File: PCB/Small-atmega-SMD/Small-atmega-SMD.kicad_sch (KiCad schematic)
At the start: 30 parts, among them J1 Daisy port in, J2 ICSP_ISP6, J3 UART, J4 Daisy port out, K1 HYC77-TF09-200, U1 PC817C-S, U2 SE5218, U21 TXB0104QPWRQ1, U3 ATmega328P-AU, Y1 16MHz

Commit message: Move connector away from MCU
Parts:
- J1: footprint Connector_IDC:IDC-Header_2x10_P2.54mm_Vertical -> Connector_IDC:IDC-Header_2x10_P2.54mm_Horizontal
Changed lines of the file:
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@@
 			)
 		)
-		(property "Footprint" "Connector_IDC:IDC-Header_2x10_P2.54mm_Vertical"
+		(property "Footprint" "Connector_IDC:IDC-Header_2x10_P2.54mm_Horizontal"
 			(at 33.02 31.75 0)
 			(effects

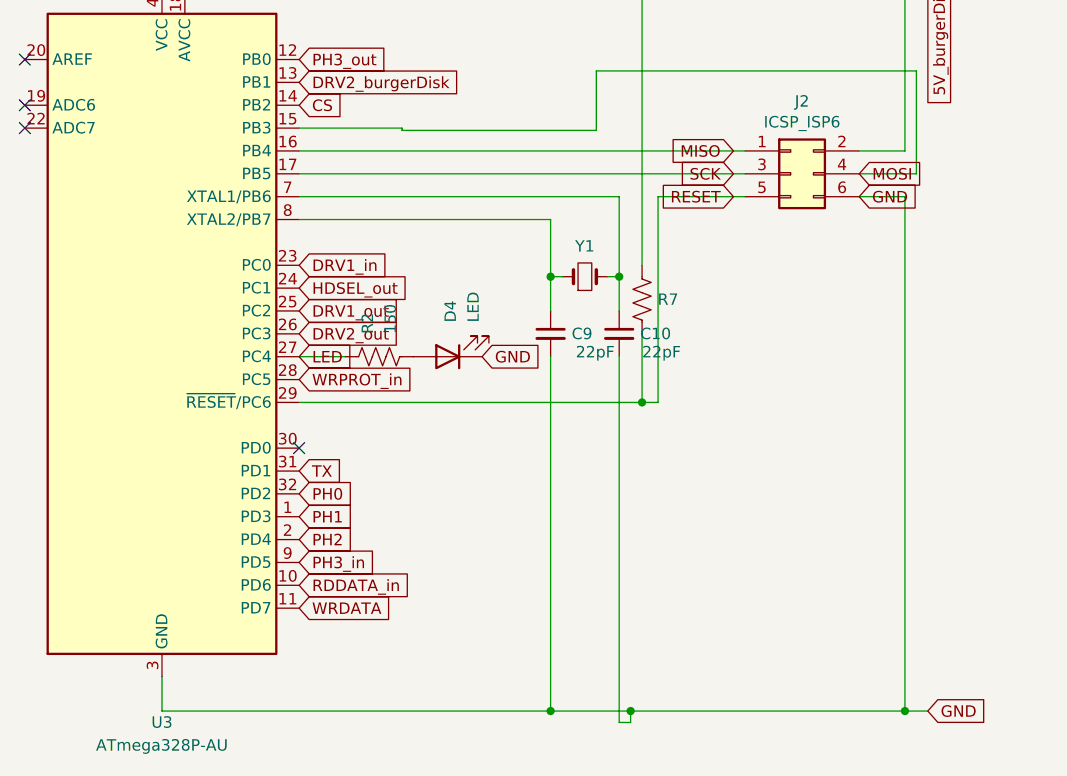
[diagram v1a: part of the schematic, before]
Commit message: Switch to resonator
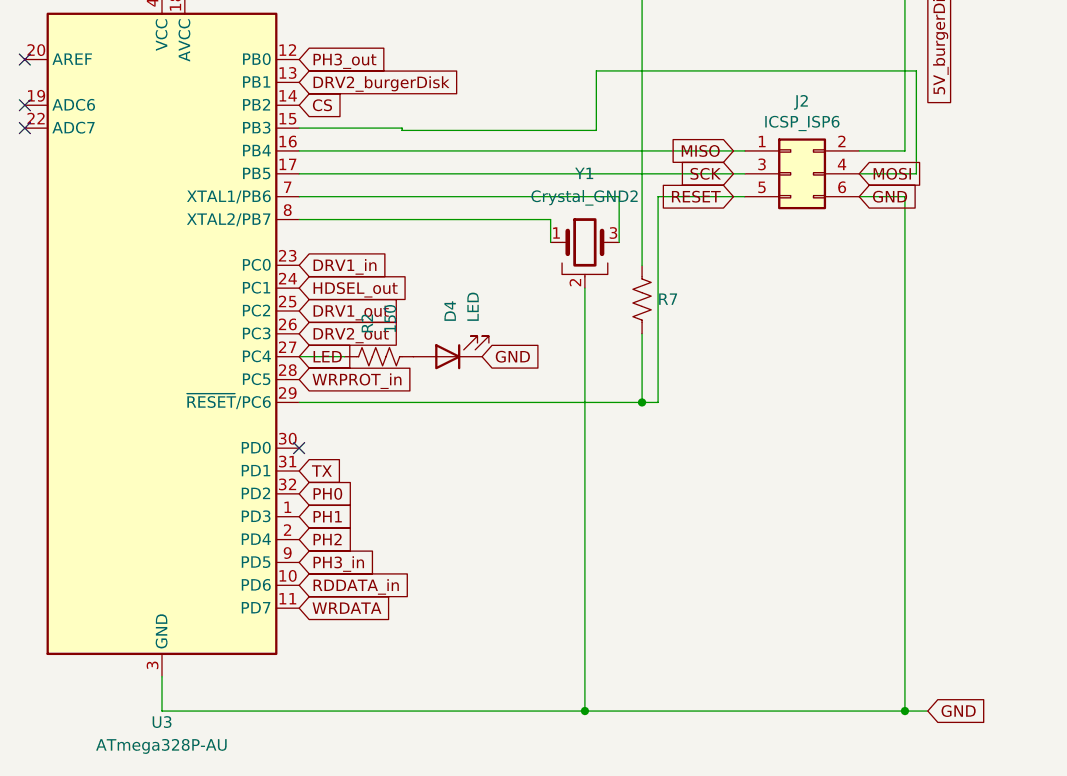
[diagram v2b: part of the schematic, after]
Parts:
- removed C10, C9: 22pF, Capacitor_SMD:C_0603_1608Metric, symbol Device:C_Small
- removed Y1: 16MHz, Crystal:Crystal_SMD_HC49-SD, symbol Device:Crystal_Small
- added Y1: Crystal_GND2, Crystal:Resonator_SMD_Murata_CSTxExxV-3Pin_3.0x1.1mm, symbol Device:Crystal_GND2
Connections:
- net GND: now also Y1.2
- net at U3.8 (XTAL2/PB7): now also Y1.1
- net at U3.7 (XTAL1/PB6): now also Y1.3

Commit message: Rework for cleanliness
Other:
- note removed: "HEADER"

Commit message: Fix part number on Small version
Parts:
- J1: LCSC C3405 -> C9144
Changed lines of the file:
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@@
 			)
 		)
-		(property "LCSC" "C3405"
+		(property "LCSC" "C9144"
 			(at 33.02 31.75 0)
 			(effects

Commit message: Fix LCSC parts
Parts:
- R7: LCSC C17414 -> C177337
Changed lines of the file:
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@@
 			)
 		)
-		(property "LCSC" "C17414"
+		(property "LCSC" "C177337"
 			(at 113.03 127 0)
 			(effects

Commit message: Add libraries and update Domino/Angled
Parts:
- K1: footprint MICROSD-HYC77-TF09-200:MICROSD-HYC77-TF09-200 -> HYC04-TF09-200:MICROSD-HYC77-TF09-200
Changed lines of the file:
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@@
 			)
 		)
-		(property "Footprint" "MICROSD-HYC77-TF09-200:MICROSD-HYC77-TF09-200"
+		(property "Footprint" "HYC04-TF09-200:MICROSD-HYC77-TF09-200"
 			(at -86.36 54.61 0)
 			(effects

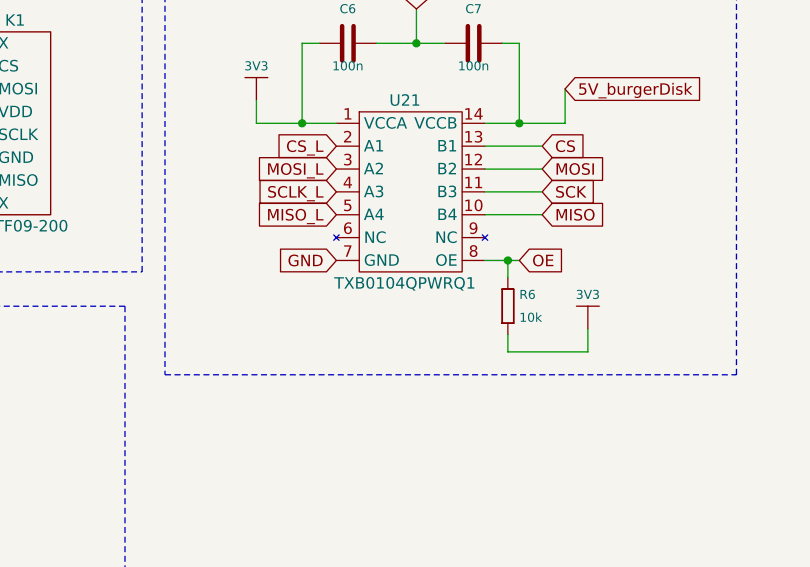
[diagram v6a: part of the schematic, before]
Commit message: Add logo (thanks to Javier Rivera!!)
Add my own micro/SD modules
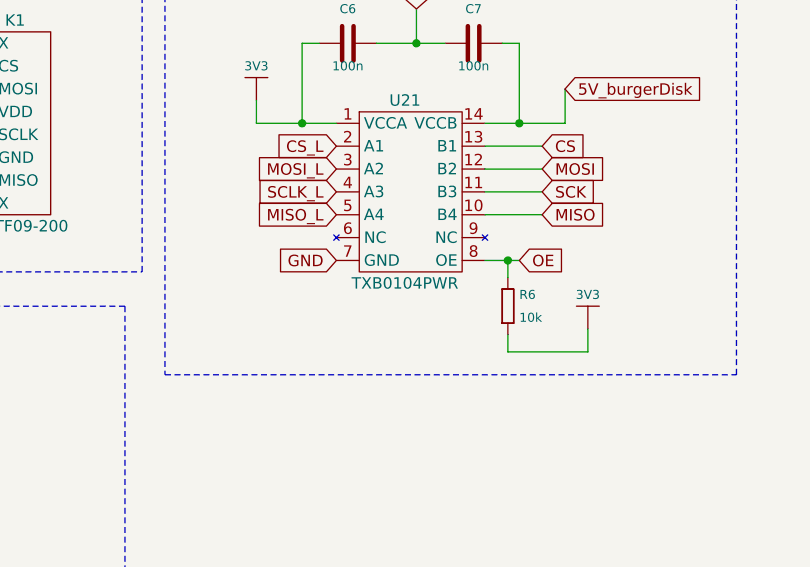
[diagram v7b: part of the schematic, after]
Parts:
- U21: value TXB0104QPWRQ1 -> TXB0104PWR; LCSC C527571 -> C60708
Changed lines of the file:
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@@
 			)
 		)
-		(property "Value" "TXB0104QPWRQ1"
+		(property "Value" "TXB0104PWR"
 			(at -43.18 58.42 0)
 			(effects
@@
 			)
 		)
-		(property "LCSC" "C527571"
+		(property "LCSC" "C60708"
 			(at -43.18 46.99 0)
 			(effects

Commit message: More OCD
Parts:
- renumbered C8 to C1, C4 to C2, C7 to C3, C6 to C4, C3 to C6, C2 to C7, C1 to C8, D3 to D1, D4 to D3, J4 to J1, J1 to J4, R5 to R1, R4 to R2, R7 to R3, R3 to R4, R6 to R5, R1 to R6, R2 to R7, U3 to U2, U2 to U3, U21 to U4
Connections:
- net GND: now also K1.SHIELD
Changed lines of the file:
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@@
+		)
+	)
+	(global_label "GND"
+		(shape input)
+		(at -80.01 30.48 270)
+		(fields_autoplaced yes)
+		(effects
+			(font
+				(size 1.27 1.27)
+			)
+			(justify right)
+		)
+		(property "Intersheetrefs" "${INTERSHEET_REFS}"
+			(at -80.01 37.3357 90)
+			(effects
+				(font
+					(size 1.27 1.27)
+				)
+				(justify right)
+				(hide yes)
+			)
 		)
 	)
@@
 		(on_board yes)
 		(dnp no)
-		(property "Reference" "C6"
+		(property "Reference" "C4"
 			(at -49.53 27.94 0)
 			(effects
@@
 			(project "Small"
 				(path "/596d0583-1d97-453e-b84c-75eed809afa2"
-					(reference "C6")
+					(reference "C4")
 					(unit 1)
 				)
@@
 		(on_board yes)
 		(dnp no)
-		(property "Reference" "C8"
+		(property "Reference" "C1"
 			(at 31.75 102.87 90)
 			(effects
@@
 			(project "Small-atmega-SMD"
 				(path "/596d0583-1d97-453e-b84c-75eed809afa2"
-					(reference "C8")
+					(reference "C1")
 					(unit 1)
 				)
@@
 		(dnp no)
 		(fields_autoplaced yes)
-		(property "Reference" "J4"
+		(property "Reference" "J1"
 			(at 241.3 107.95 0)
 			(effects
@@
 			(project "BurgerDisk_THT_AngledDB19"
 				(path "/596d0583-1d97-453e-b84c-75eed809afa2"
-					(reference "J4")
+					(reference "J1")
 					(unit 1)
 				)
@@
 		(on_board yes)
 		(dnp no)
-		(property "Reference" "U3"
+		(property "Reference" "U2"
 			(at 59.69 173.99 0)
 			(effects
@@
 			(project "Small-atmega-SMD"
 				(path "/596d0583-1d97-453e-b84c-75eed809afa2"
-					(reference "U3")
+					(reference "U2")
 					(unit 1)
 				)
@@
 		(on_board yes)
 		(dnp no)
-		(property "Reference" "U2"
+		(property "Reference" "U3"
 			(at -107.95 91.44 0)
 			(effects
@@
 			(project "Small"
 				(path "/596d0583-1d97-453e-b84c-75eed809afa2"
-					(reference "U2")
+					(reference "U3")
 					(unit 1)
 				)
@@
 		(on_board yes)
 		(dnp no)
-		(property "Reference" "R4"
+		(property "Reference" "R2"
 			(at 101.6 55.88 0)
 			(effects
@@
 			(project "BurgerDisk_THT_AngledDB19"
 				(path "/596d0583-1d97-453e-b84c-75eed809afa2"
-					(reference "R4")
+					(reference "R2")
 					(unit 1)
 				)
@@
 		(on_board yes)
 		(dnp no)
-		(property "Reference" "C1"
+		(property "Reference" "C8"
 			(at -125.73 39.37 90)
 			(effects
@@
 			(project "Small"
 				(path "/596d0583-1d97-453e-b84c-75eed809afa2"
-					(reference "C1")
+					(reference "C8")
 					(unit 1)
 				)
@@
 		(pin "8"
 		)
+		(pin "SHIELD"
+		)
 		(instances
 			(project "Small"
@@
 		(on_board yes)
 		(dnp no)
-		(property "Reference" "R6"
+		(property "Reference" "R5"
 			(at -30.48 59.69 90)
 			(effects
@@
 			(project "Small"
 				(path "/596d0583-1d97-453e-b84c-75eed809afa2"
-					(reference "R6")
+					(reference "R5")
 					(unit 1)
 				)
@@
 		(on_board yes)
 		(dnp no)
-		(property "Reference" "R7"
+		(property "Reference" "R3"
 			(at 114.7572 127 0)
 			(effects
@@
 			(project "Small-atmega-SMD"
 				(path "/596d0583-1d97-453e-b84c-75eed809afa2"
-					(reference "R7")
+					(reference "R3")
 					(unit 1)
 				)
@@
 		(dnp no)
 		(fields_autoplaced yes)
-		(property "Reference" "R3"
+		(property "Reference" "R4"
 			(at 119.38 27.94 0)
 			(effects
@@
 			(project "BurgerDisk_THT_AngledDB19"
 				(path "/596d0583-1d97-453e-b84c-75eed809afa2"
-					(reference "R3")
+					(reference "R4")
 					(unit 1)
 				)
@@
 		(dnp no)
 		(fields_autoplaced yes)
-		(property "Reference" "D4"
+		(property "Reference" "D3"
 			(at 91.7575 129.54 90)
 			(effects
@@
 			(project "Small-atmega-SMD"
 				(path "/596d0583-1d97-453e-b84c-75eed809afa2"
-					(reference "D4")
+					(reference "D3")
 					(unit 1)
 				)
@@
 		(dnp no)
 		(fields_autoplaced yes)
-		(property "Reference" "J1"
+		(property "Reference" "J4"
 			(at 34.29 15.24 0)
 			(effects
@@
 			(project "BurgerDisk_THT_AngledDB19"
 				(path "/596d0583-1d97-453e-b84c-75eed809afa2"
-					(reference "J1")
+					(reference "J4")
 					(unit 1)
 				)
@@
 		(on_board yes)
 		(dnp no)
-		(property "Reference" "C2"
+		(property "Reference" "C7"
 			(at -118.11 39.37 90)
 			(effects
@@
 			(project "Small"
 				(path "/596d0583-1d97-453e-b84c-75eed809afa2"
-					(reference "C2")
+					(reference "C7")
 					(unit 1)
 				)
@@
 		(on_board yes)
 		(dnp no)
-		(property "Reference" "C3"
+		(property "Reference" "C6"
 			(at -110.49 39.37 90)
 			(effects
@@
 			(project "Small"
 				(path "/596d0583-1d97-453e-b84c-75eed809afa2"
-					(reference "C3")
+					(reference "C6")
 					(unit 1)
 				)
@@
 		(dnp no)
 		(fields_autoplaced yes)
-		(property "Reference" "R2"
+		(property "Reference" "R7"
 			(at 82.55 130.81 0)
 			(effects
@@
 			(project "Small-atmega-SMD"
 				(path "/596d0583-1d97-453e-b84c-75eed809afa2"
-					(reference "R2")
+					(reference "R7")
 					(unit 1)
 				)
@@
 		(on_board yes)
 		(dnp no)
-		(property "Reference" "C4"
+		(property "Reference" "C2"
 			(at -120.65 96.52 90)
 			(effects
@@
 			(project "Small"
 				(path "/596d0583-1d97-453e-b84c-75eed809afa2"
-					(reference "C4")
+					(reference "C2")
 					(unit 1)
 				)
@@
 		(on_board yes)
 		(dnp no)
-		(property "Reference" "R1"
+		(property "Reference" "R6"
 			(at 29.21 50.8 0)
 			(effects
@@
 			(project "BurgerDisk_THT_AngledDB19"
 				(path "/596d0583-1d97-453e-b84c-75eed809afa2"
-					(reference "R1")
+					(reference "R6")
 					(unit 1)
 				)
@@
 		(dnp no)
 		(fields_autoplaced yes)
-		(property "Reference" "D3"
+		(property "Reference" "D1"
 			(at 149.5425 83.82 0)
 			(effects
@@
 			(project "Small-atmega-SMD"
 				(path "/596d0583-1d97-453e-b84c-75eed809afa2"
-					(reference "D3")
+					(reference "D1")
 					(unit 1)
 				)
@@
 		(on_board yes)
 		(dnp no)
-		(property "Reference" "C7"
+		(property "Reference" "C3"
 			(at -35.56 27.94 0)
 			(effects
@@
 			(project "Small"
 				(path "/596d0583-1d97-453e-b84c-75eed809afa2"
-					(reference "C7")
+					(reference "C3")
 					(unit 1)
 				)
@@
 		(on_board yes)
 		(dnp no)
-		(property "Reference" "U21"
+		(property "Reference" "U4"
 			(at -43.18 38.1 0)
 			(effects
@@
 			(project "Small"
 				(path "/596d0583-1d97-453e-b84c-75eed809afa2"
-					(reference "U21")
+					(reference "U4")
 					(unit 1)
 				)
@@
 		(dnp no)
 		(fields_autoplaced yes)
-		(property "Reference" "R5"
+		(property "Reference" "R1"
 			(at 116.84 53.34 0)
 			(effects
@@
 			(project "BurgerDisk_THT_AngledDB19"
 				(path "/596d0583-1d97-453e-b84c-75eed809afa2"
-					(reference "R5")
-					(unit 1)
-				)
+					(reference "R1")
+					(unit 1)
+				)
